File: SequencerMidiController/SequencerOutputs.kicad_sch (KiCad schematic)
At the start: 32 parts, among them J4 Conn_02x10_Odd_Even, SW7 SW_SPST, U34 ADG2188

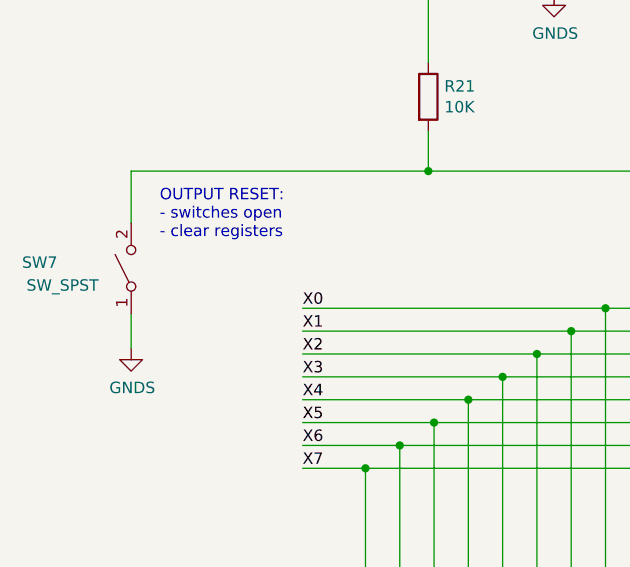
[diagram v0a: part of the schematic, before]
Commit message: updated user buttons
removed dipsw, added four more tactile button (three above display, three below display, six total)
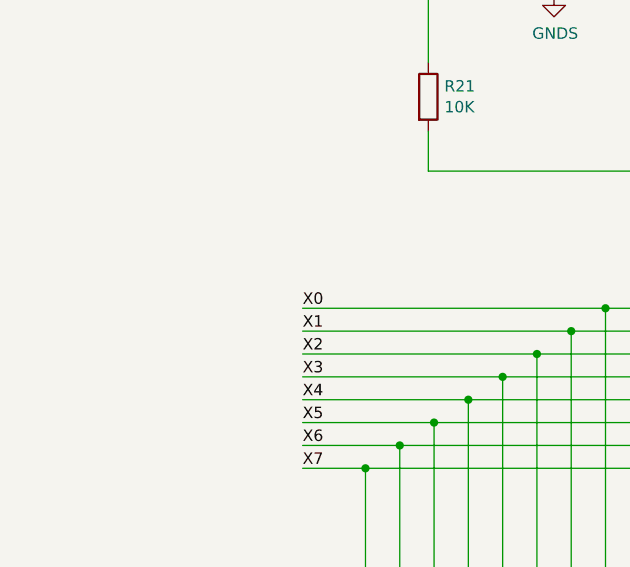
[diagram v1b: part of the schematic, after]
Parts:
- removed SW7: SW_SPST, Button_Switch_THT:SW_PUSH-12mm, symbol Switch:SW_SPST
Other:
- note removed: "OUTPUT RESET: - switches open - clear registers"
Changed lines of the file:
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@@
   (junction (at 92.075 31.115) (diameter 0) (color 0 0 0 0)
-  )
-  (junction (at 64.135 89.535) (diameter 0) (color 0 0 0 0)
   )
   (junction (at 201.93 60.325) (diameter 0) (color 0 0 0 0)
@@
     (stroke (width 0) (type default) (color 0 0 0 0))
   )
-  (wire (pts (xy 31.115 105.41) (xy 31.115 109.22))
-    (stroke (width 0) (type default) (color 0 0 0 0))
-  )
   (wire (pts (xy 120.65 120.015) (xy 129.54 120.015))
     (stroke (width 0) (type default) (color 0 0 0 0))
@@
     (stroke (width 0) (type default) (color 0 0 0 0))
   )
-  (wire (pts (xy 31.115 95.25) (xy 31.115 89.535))
-    (stroke (width 0) (type default) (color 0 0 0 0))
-  )
   (wire (pts (xy 137.16 114.935) (xy 162.56 114.935))
     (stroke (width 0) (type default) (color 0 0 0 0))
@@
   )
   (wire (pts (xy 140.97 94.615) (xy 120.65 94.615))
-    (stroke (width 0) (type default) (color 0 0 0 0))
-  )
-  (wire (pts (xy 64.135 89.535) (xy 31.115 89.535))
     (stroke (width 0) (type default) (color 0 0 0 0))
   )
@@
   (text "The ADG2188 has a 7-bit slave address. \nThe four MSBs are hard coded to 1110, \nand the three LSBs are determined by\n the state of Pin A0, Pin A1, and Pin A2."
     (at 170.18 31.115 0)
-    (effects (font (size 1.27 1.27)) (justify left bottom))
-  )
-  (text "OUTPUT RESET:\n- switches open\n- clear registers" (at 34.29 97.155 0)
     (effects (font (size 1.27 1.27)) (justify left bottom))
   )
@@
       (effects (font (size 1.27 1.27)) hide)
     )
-    (pin "1")
-  )
-  (symbol (lib_id "Switch:SW_SPST") (at 31.115 100.33 90) (unit 1)
-    (in_bom yes) (on_board yes)
-    (property "Reference" "SW7" (id 0) (at 20.955 99.695 90))
-    (property "Value" "SW_SPST" (id 1) (at 23.495 102.235 90))
-    (property "Footprint" "Button_Switch_THT:SW_PUSH-12mm" (id 2) (at 31.115 100.33 0)
-      (effects (font (size 1.27 1.27)) hide)
-    )
-    (property "Datasheet" "~" (id 3) (at 31.115 100.33 0)
-      (effects (font (size 1.27 1.27)) hide)
-    )
-    (property "LcscNo" "~" (id 4) (at 31.115 100.33 0)
-      (effects (font (size 1.27 1.27)) hide)
-    )
-    (property "Type" "~" (id 5) (at 31.115 100.33 0)
-      (effects (font (size 1.27 1.27)) hide)
-    )
-    (pin "1")
-    (pin "2")
-  )
-  (symbol (lib_id "power:GNDS") (at 31.115 109.22 0) (unit 1)
-    (in_bom yes) (on_board yes)
-    (property "Reference" "#PWR039" (id 0) (at 31.115 115.57 0)
-      (effects (font (size 1.27 1.27)) hide)
-    )
-    (property "Value" "GNDS" (id 1) (at 31.242 113.6142 0))
-    (property "Footprint" "" (id 2) (at 31.115 109.22 0)
-      (effects (font (size 1.27 1.27)) hide)
-    )
-    (property "Datasheet" "" (id 3) (at 31.115 109.22 0)
-      (effects (font (size 1.27 1.27)) hide)
-    )
